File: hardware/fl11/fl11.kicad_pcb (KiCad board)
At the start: 2 copper layers, 187 x 52 mm, 80 parts, among them J1 USB-C 16P, J2 SENSE+GND, J3_1 TOUCH_SENSE, J3_2 GND, J4 5V/GND/SIG, Q1 AO3401A, SW1 BOOT, U1 ESP32-C3-MINI-1-N4, U2 SN74AHCT1G125, U3 AP2112K-3.3, U4 USBLC6-2SC6

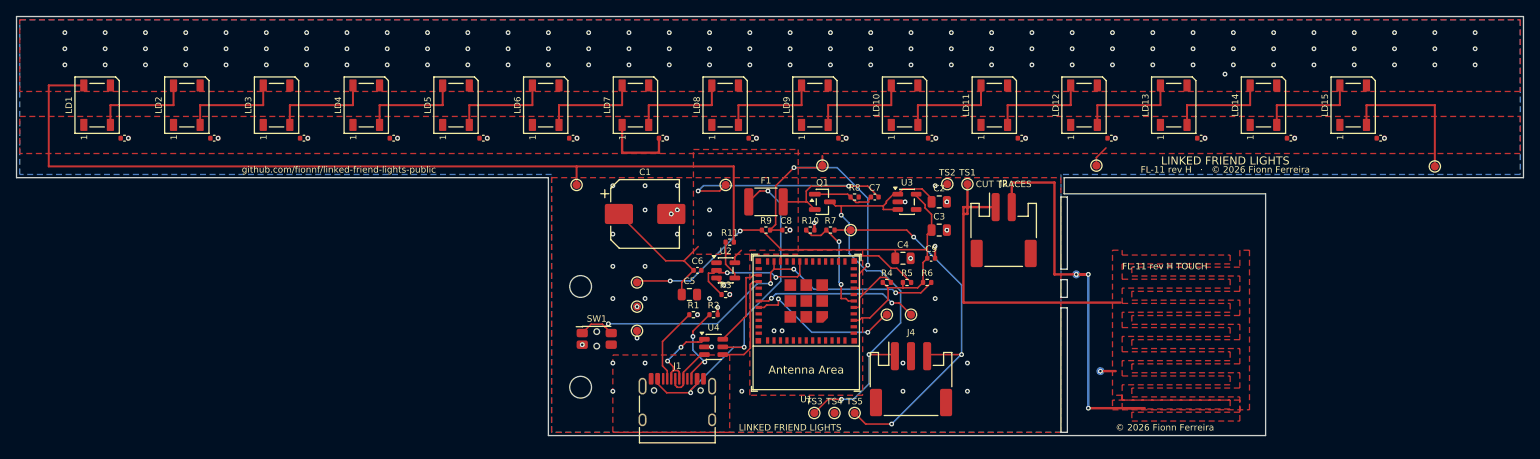
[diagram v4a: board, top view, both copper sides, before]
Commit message: FL-11 rev I: a TTP223 module replaces the etched sensor
This is the biggest simplification in the design. A TTP223-class module plugs
into J4 in IO / VCC / GND order and does the sensing, which deletes the comb
electrodes, the snap-off pad section, the break line, the webs, both bridges,
and R10's 4.7M -- the thinnest-stock line on the BOM, now a 100k that was
already there. It also deletes section 7.5's entire uncertainty: the
charge-time measurement, the per-unit threshold, the overlay dependence, and
the note calling touch the least-certain subsystem in the design. touch.py
becomes a digital read.

VCC is 3V3 and not 5V on purpose. These modules drive their output
rail-to-rail and the ESP32-C3 is not 5V tolerant at 3.6 V absolute max, so a
5V-powered module would overdrive IO3. R7's 5.1k stays in series anyway.
TS3/TS4/TS5 repeat the three signals as solder terminals.

Centred geometry as asked: the LED row has 15.567 mm of headroom at each end,
identical, and the USB-C sits dead centre of the bulge at x=98.0. The module
moved aside to x=115 to make room, which leaves its antenna keep-out facing
the free y=52 edge, 23.9 mm from the nearest LED copper against a rule of 8.

Four screws now: two in the bulge and one at each end of the LED strip, so the
whole length is held rather than just the electronics.

0 DRC errors, 0 unconnected pads, 16 BOM lines, 59 placements, single-sided.

Co-Authored-By: Claude Opus 5 (1M context) <noreply@anthropic.com>
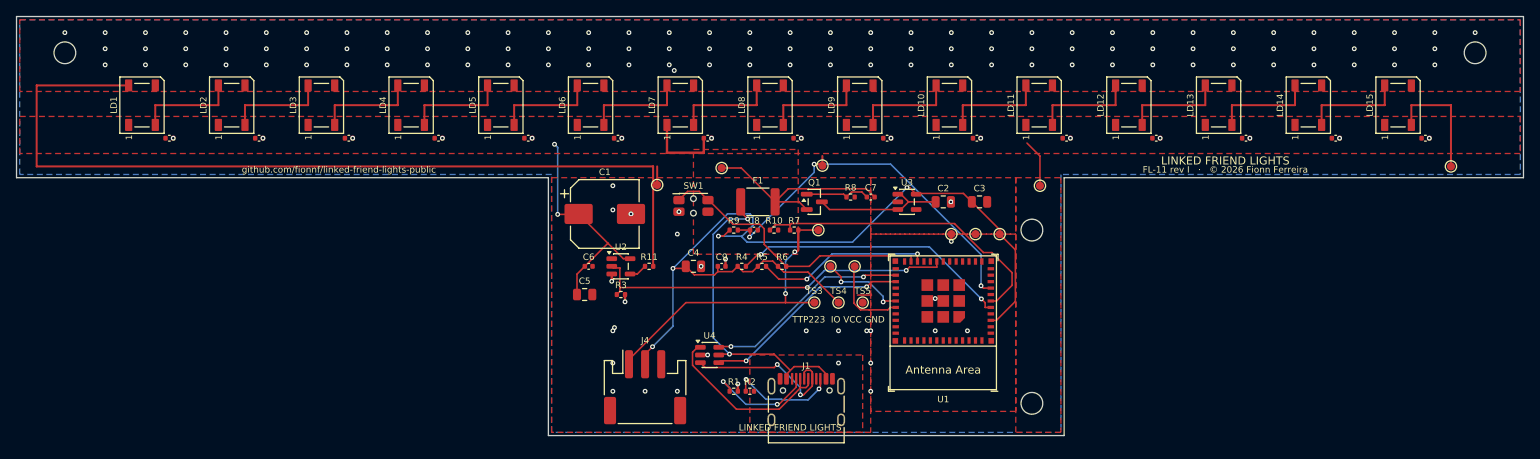
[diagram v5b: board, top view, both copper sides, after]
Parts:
- removed J2: SENSE+GND, JST_PH_S2B-PH-SM4-TB_1x02-1MP_P2.00mm_Horizontal
- removed J3_1, TS1: TOUCH_SENSE, TestPoint_Pad_D1.0mm
- removed J3_2, TS2: GND, TestPoint_Pad_D1.0mm
- added H3: M2.5, MountingHole_2.7mm_M2.5, F.Cu at (6.00, 4.50)
- added H4: M2.5, MountingHole_2.7mm_M2.5, F.Cu at (181.0, 4.50)
- J4: value 5V/GND/SIG -> IO/VCC/GND
- R10: value 4M7 -> 100k
- TS3: value +5V -> TOUCH_SENSE
- TS4: value GND -> +3V3
- TS5: value TOUCH_SENSE -> GND
- moved H2 56.4 mm to (126.0, 26.5)
- moved H1 56.0 mm to (126.0, 48.0)
- moved TP2 45.4 mm to (122.0, 27.0)
- moved TP3 43.0 mm to (119.0, 27.0)
- moved TP4 40.8 mm to (116.0, 27.0)
- moved J4 33.0 mm to (78.0, 46.0)
- moved C4 26.0 mm to (84.0, 31.0)
- moved C9 26.0 mm to (87.5, 31.0)
- moved SW1 20.4 mm to (84.0, 23.5)
- moved R4 18.1 mm to (90.0, 31.0)
- moved R5 18.1 mm to (92.5, 31.0)
- moved R6 18.1 mm to (95.0, 31.0)
- moved U1 17.0 mm to (115.0, 38.0)
- moved J1 16.0 mm to (98.0, 49.0)
- moved TS5 13.7 mm to (105.0, 35.5)
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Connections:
- J4 pad 1: +5V -> TOUCH_SENSE
- J4 pad 2: GND -> +3V3
- J4 pad 3: TOUCH_SENSE -> GND
- TS3 pad 1: +5V -> TOUCH_SENSE
- TS4 pad 1: GND -> +3V3
- TS5 pad 1: TOUCH_SENSE -> GND
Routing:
- net TOUCH_SENSE: track 90.4 -> 38.8 mm, vias 4 -> 2
- net GND: track 56.3 -> 7.15 mm, vias 170 -> 149
- net +3V3: track 66.0 -> 110.0 mm, vias 2 -> 4
- net +5V: track 56.3 -> 16.6 mm, vias 3 -> 0
- net LED_DATA_3V3: track 16.9 -> 45.6 mm
- net STRAP2: track 7.10 -> 34.8 mm, vias 0 -> 2
- net TOUCH_GPIO: track 14.1 -> 38.6 mm, vias 2 -> 0
- net BOOT_N: track 51.4 -> 35.5 mm, vias 4 -> 0
- net USB_DM: track 10.5 -> 25.7 mm, vias 0 -> 2
- net USB_DP_CONN: track 7.13 -> 20.6 mm, vias 0 -> 2
- net USB_DP: track 12.8 -> 26.1 mm, vias 0 -> 2
- net USB_DM_CONN: track 9.98 -> 22.6 mm, vias 2 -> 0
- net VBUS_F: track 38.2 -> 26.1 mm, vias 2 -> 0
- net LED_5V: track 32.7 -> 43.9 mm, vias 0 -> 2
- net UART_RX: track 20.4 -> 10.7 mm
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- removed copper zone on F.Cu, net TOUCH_SENSE
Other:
- outline, holes or cut-outs redrawn
- board text added: "FL-11 rev I · © 2026 Fionn Ferreira"
- board text added: "TTP223 IO VCC GND"
- board text removed: "CUT TRACES"
- board text removed: "FL-11 rev H TOUCH"
- board text removed: "FL-11 rev H · © 2026 Fionn Ferreira"
- board text removed: "© 2026 Fionn Ferreira"
